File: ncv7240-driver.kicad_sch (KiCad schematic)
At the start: 0 parts

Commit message: Draw block-diagram schematic with all symbols embedded for kicanvas
- Python generator at tools/gen_sch.py produces ncv7240-driver.kicad_sch
- All symbol definitions embedded inline (kicanvas has no external libs)
- Components: USB-C, AP33772S, ESP32-S3-WROOM-1, 4x NCV7240, buck reg,
  bulk/decoupling caps, TVS, pull-ups, 8-pin output screw terminals
- Connectivity via KiCad global labels (SPI bus, I2C, power rails, OUT1..32)
- A2 sheet, deterministic UUIDs for clean diffs
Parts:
- added C1: 100uF/50V, symbol Device:C
- added C10, C12, C14, C16, C5: 100nF, symbol Device:C
- added C11, C13, C15, C17, C2: 10uF/50V, symbol Device:C
- added C3, C4: 10uF, symbol Device:C
- added D1: SMBJ33A, symbol Device:D_TVS
- added J1: USB-C EPR, Connector:USB_C_Receptacle_HRO_TYPE-C-31-M-12, symbol Connector:USB_C
- added J2: OUT1..8, TerminalBlock:TerminalBlock_Phoenix_MKDS-1,5-8_1x08_P5.00mm_Horizontal, symbol Connector:Screw_Term_8
- added J3: OUT9..16, TerminalBlock:TerminalBlock_Phoenix_MKDS-1,5-8_1x08_P5.00mm_Horizontal, symbol Connector:Screw_Term_8
- added J4: OUT17..24, TerminalBlock:TerminalBlock_Phoenix_MKDS-1,5-8_1x08_P5.00mm_Horizontal, symbol Connector:Screw_Term_8
- added J5: OUT25..32, TerminalBlock:TerminalBlock_Phoenix_MKDS-1,5-8_1x08_P5.00mm_Horizontal, symbol Connector:Screw_Term_8
- added L1: 4.7uH, symbol Device:L
- added R1, R2, R3: 10k, symbol Device:R
- added R4, R5: 4.7k, symbol Device:R
- added R6: 100k, symbol Device:R
- added R7: 20k, symbol Device:R
- added U1: AP33772S, Package_DFN_QFN:QFN-24-1EP_4x4mm_P0.5mm_EP2.6x2.6mm, symbol PMIC:AP33772S
- added U2: ESP32-S3-WROOM-1-N8R8, RF_Module:ESP32-S2-WROOM, symbol RF_Module:ESP32-S3-WROOM-1
- added U3, U4, U5, U6: NCV7240, Package_SO:SSOP-24_5.3x8.2mm_P0.65mm, symbol Driver_Motor:NCV7240
- added U7: TPS62932, Package_TO_SOT_SMD:SOT-23-6, symbol Regulator_Switching:BUCK_24_3V3
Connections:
- new net: R6.1, R7.2
- new net +24V: C1.1, C10.1, C11.1, C12.1, C13.1, C14.1, C15.1, C16.1, C17.1, C2.1
- new net +3V3: C3.1, C4.1, C5.1, R1.1, R2.1, R3.1, R4.1, R5.1
- new net GND: C1.2, C10.2, C11.2, C12.2, C13.2, C14.2, C15.2, C16.2, C17.2, C2.2, C3.2, C4.2, C5.2
- new net I2C_SCL: R5.2
- new net I2C_SDA: R4.2
- new net NCV_FSOB: R3.2
- new net NCV_RSTB: R2.2
- new net SPI_MISO: R1.2
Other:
- note added: "24V → 3.3V buck"
- note added: "4× NCV7240 — 32 low-side outputs @ 24V"
- note added: "AP33772S: 1uF on VDD, 100nF on VPP (place close to IC pins, not shown here)"
- note added: "Antenna keep-out ≥15mm under module top edge"
- note added: "Buck 24V→3.3V, ≥500mA VOUT = 0.6V·(1+R6/R7)"
- note added: "ESP32-S3-WROOM-1 (Wi-Fi/BT, USB-OTG)"
- note added: "USB-C PD 3.1 EPR sink — 24V/3A negotiated"

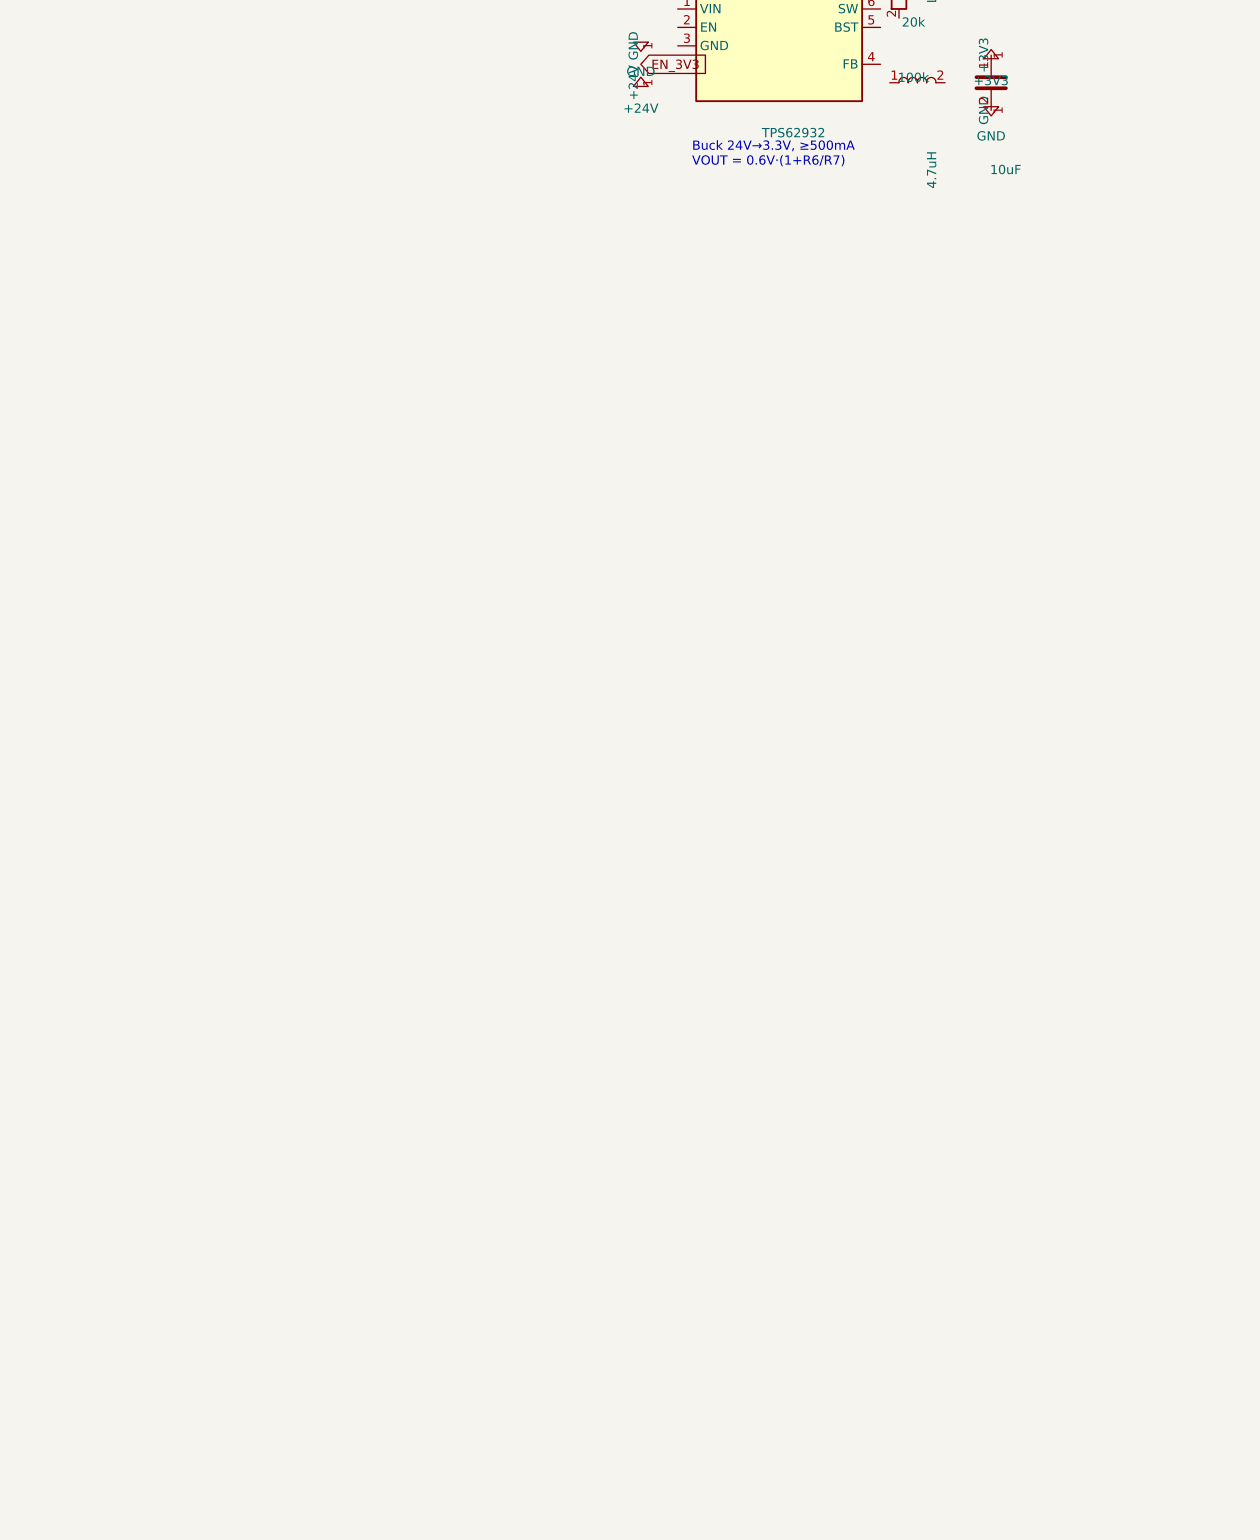
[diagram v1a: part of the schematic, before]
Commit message: Add 32 flyback diodes, real footprints, and parts datasheets
- 32× B260A-13-F Schottky (60V / 2A SMA) freewheel diodes — one per
  output, anode→OUTx, cathode→+24V, for Bürkert Type 0127 valve coils
  (3 W @ 24 V ≈ 125 mA, inductive)
- Footprints assigned for all parts:
    - NCV7240         SSOP-24 P0.65
    - AP33772S        QFN-24 4x4 EP2.6
    - ESP32-S3-WROOM-1 (fixed from S2 typo)
    - USB-C           HRO TYPE-C-31-M-12
    - Buck            SOT-23-6
    - L1              Bourns SRN6045 4.7uH
    - Bulk caps       CP_Elec_10x10.5 / C_1210
    - Decoupling      C_0603 / C_0805
    - Resistors       R_0603
    - TVS             SMB
    - Flyback diodes  SMA
    - Screw terminals Phoenix MKDS-1,5 8-pos
- datasheets/ committed (NCV7240, AP33772S, ESP32-S3-WROOM-1, B260A,
  Bürkert 0127)
- Schematic now 2406 lines, 32 freewheel diodes verified
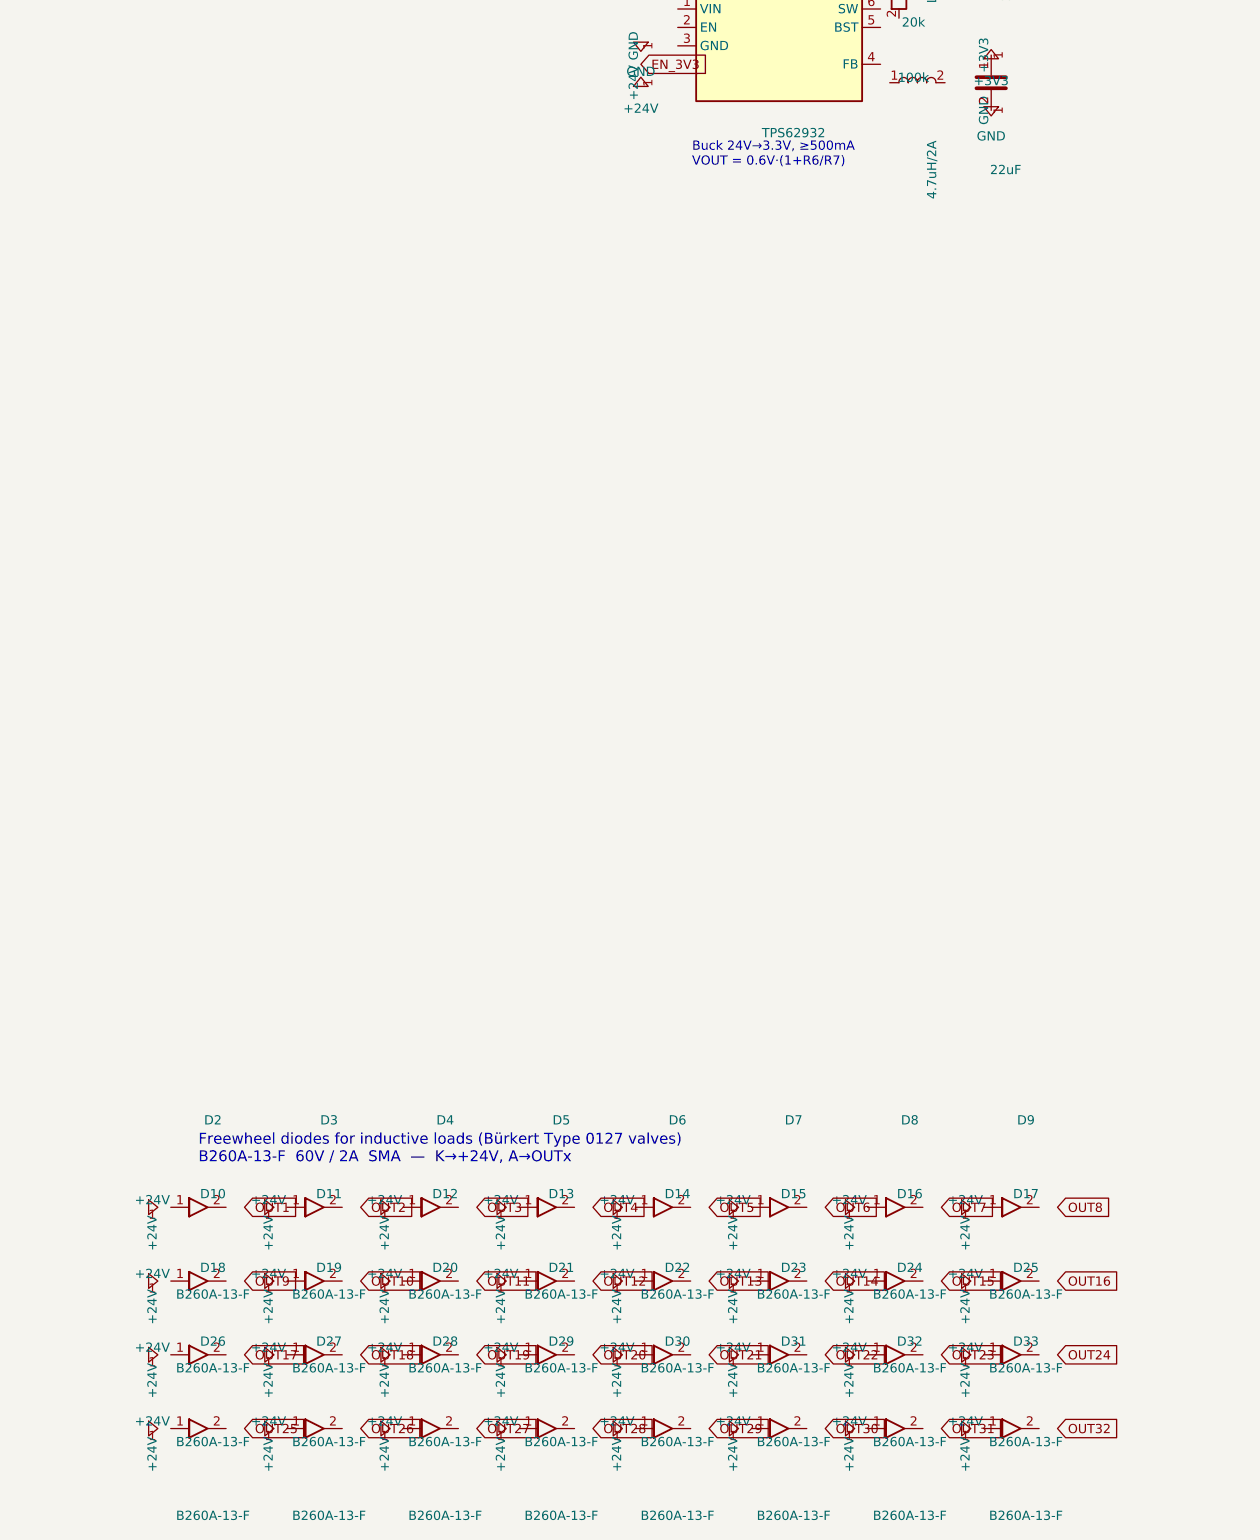
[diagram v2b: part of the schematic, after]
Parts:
- added D10, D11, D12, D13, D14, D15, D16, D17, D18, D19, D2, D20, D21, D22, D23, D24, D25, D26, D27, D28, D29, D3, D30, D31, D32, D33, D4, D5, D6, D7, D8, D9: B260A-13-F, Diode_SMD:D_SMA, symbol Device:D
- C1: footprint (none) -> Capacitor_SMD:CP_Elec_10x10.5
- C10, C12, C14, C16, C5: footprint (none) -> Capacitor_SMD:C_0603_1608Metric
- C11, C13, C15, C17, C2: footprint (none) -> Capacitor_SMD:C_1210_3225Metric
- C3: value 10uF -> 22uF; footprint (none) -> Capacitor_SMD:C_0805_2012Metric
- C4: footprint (none) -> Capacitor_SMD:C_0805_2012Metric
- D1: footprint (none) -> Diode_SMD:D_SMB
- L1: value 4.7uH -> 4.7uH/2A; footprint (none) -> Inductor_SMD:L_Bourns-SRN6045TA
- R1, R2, R3, R4, R5, R6, R7: footprint (none) -> Resistor_SMD:R_0603_1608Metric
- U2: footprint RF_Module:ESP32-S2-WROOM -> RF_Module:ESP32-S3-WROOM-1
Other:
- note added: "Freewheel diodes for inductive loads (Bürkert Type 0127 valves) B260A-13-F 60V / 2A SMA — K→+24V, A→OUTx"
